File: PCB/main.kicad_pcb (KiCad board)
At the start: 2 copper layers, 51 parts, among them J1 S20B-PADSS-1, J2 S20B-PADSS-1, J3 SWD, SW1 SPST, U1 LM2596-5.0, U2 XC6206P33, U3 MCP2558FD, U4 MCP2558FD, U5 STM32G0B1, Y1 40M

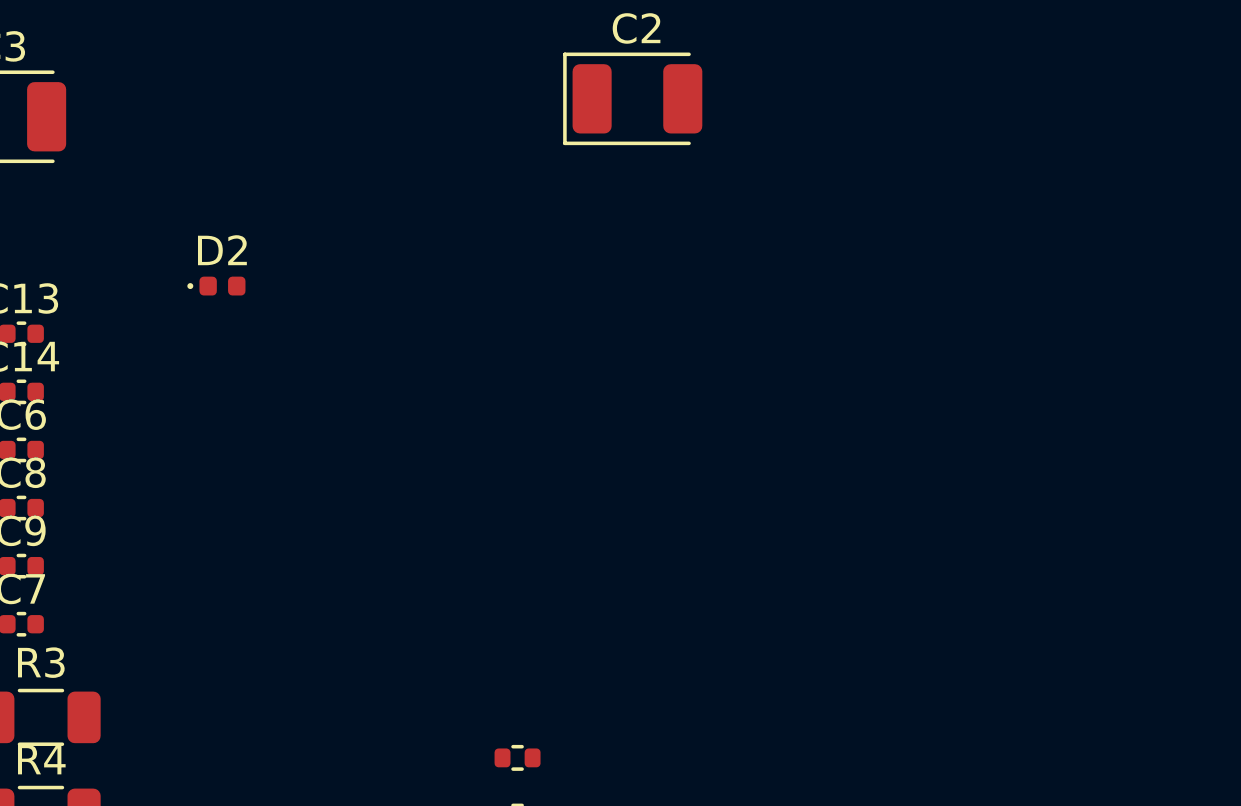
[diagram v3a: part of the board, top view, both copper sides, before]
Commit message: Add fuse holder
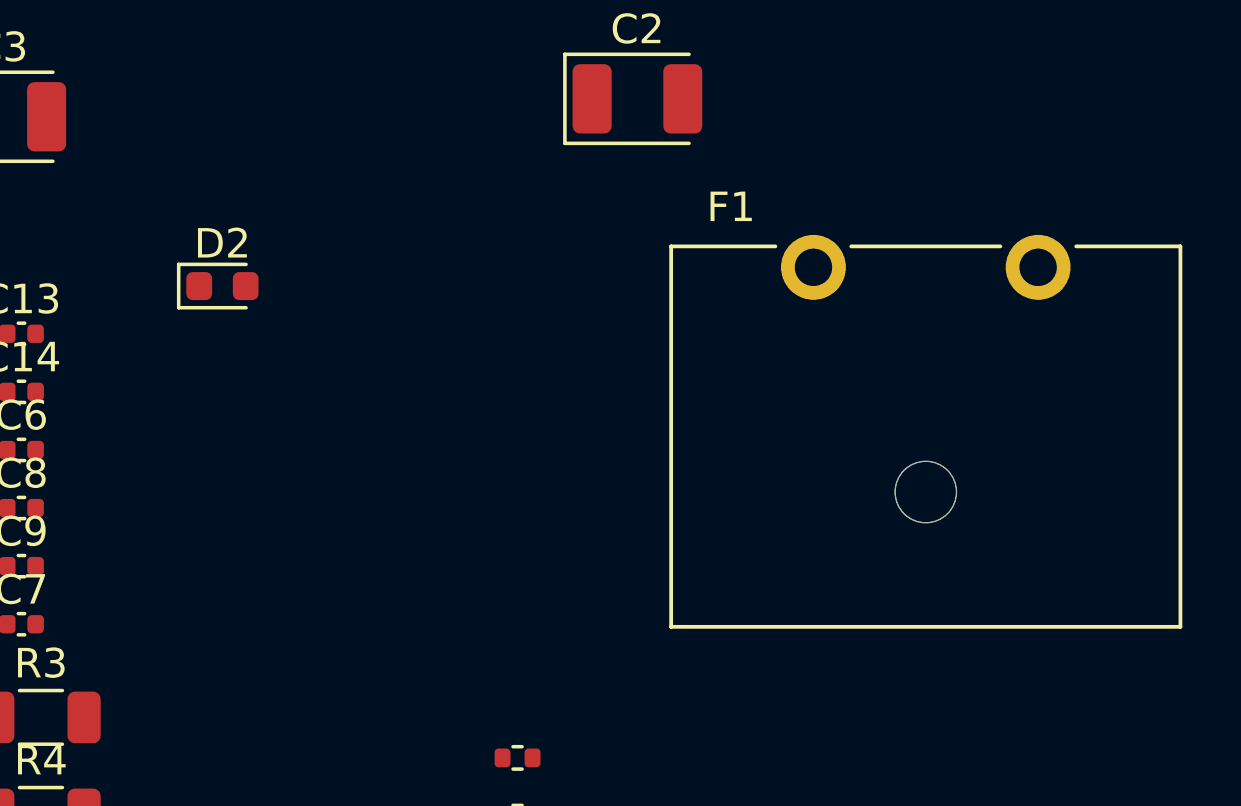
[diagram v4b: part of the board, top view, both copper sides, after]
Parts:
- added F1: Fuse, libdb:CMP-0026, F.Cu at (91.4, 35.6)
- D2: footprint LED_SMD:LED_0402_1005Metric -> LED_SMD:LED_0603_1608Metric
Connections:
- J1 pad 10: +BATT -> /JST_10_BAT+
- J2 pad 1: +BATT -> /JST_10_BAT+
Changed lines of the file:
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@@
   (net 82 "unconnected-(U5-PB8-Pad47)")
   (net 83 "unconnected-(U5-PB9-Pad48)")
+  (net 84 "/JST_10_BAT+")
   (footprint "Package_TO_SOT_SMD:TO-263-5_TabPin3" (layer "F.Cu")
     (at 28.841 47.733)
@@
     )
   )
-  (footprint "LED_SMD:LED_0402_1005Metric" (layer "F.Cu")
+  (footprint "LED_SMD:LED_0603_1608Metric" (layer "F.Cu")
     (at 67.587 28.575)
-    (descr "LED SMD 0402 (1005 Metric), square (rectangular) end terminal, IPC_7351 nominal, (Body size source: http://www.tortai-tech.com/upload/download/2011102023233369053.pdf), generated with kicad-footprint-generator")
+    (descr "LED SMD 0603 (1608 Metric), square (rectangular) end terminal, IPC_7351 nominal, (Body size source: http://www.tortai-tech.com/upload/download/2011102023233369053.pdf), generated with kicad-footprint-generator")
     (tags "LED")
     (property "Case/Package Size" "0603")
@@
     (property "ki_keywords" "LED diode light-emitting-diode")
     (attr smd)
-    (fp_text reference "D2" (at 0 -1.17) (layer "F.SilkS")
+    (fp_text reference "D2" (at 0 -1.43) (layer "F.SilkS")
         (effects (font (size 1 1) (thickness 0.15)))
     )
-    (fp_text value "LED_B" (at 0 1.17) (layer "F.Fab")
+    (fp_text value "LED_B" (at 0 1.43) (layer "F.Fab")
         (effects (font (size 1 1) (thickness 0.15)))
     )
     (fp_text user "${REFERENCE}" (at 0 0) (layer "F.Fab")
-        (effects (font (size 0.25 0.25) (thickness 0.04)))
+        (effects (font (size 0.4 0.4) (thickness 0.06)))
     )
-    (fp_circle (center -1.09 0) (end -1.04 0)
-      (stroke (width 0.1) (type solid)) (fill none) (layer "F.SilkS"))
-    (fp_line (start -0.93 -0.47) (end 0.93 -0.47)
+    (fp_line (start -1.485 -0.735) (end -1.485 0.735)
+      (stroke (width 0.12) (type solid)) (layer "F.SilkS"))
+    (fp_line (start -1.485 0.735) (end 0.8 0.735)
+      (stroke (width 0.12) (type solid)) (layer "F.SilkS"))
+    (fp_line (start 0.8 -0.735) (end -1.485 -0.735)
+      (stroke (width 0.12) (type solid)) (layer "F.SilkS"))
+    (fp_line (start -1.48 -0.73) (end 1.48 -0.73)
       (stroke (width 0.05) (type solid)) (layer "F.CrtYd"))
-    (fp_line (start -0.93 0.47) (end -0.93 -0.47)
+    (fp_line (start -1.48 0.73) (end -1.48 -0.73)
       (stroke (width 0.05) (type solid)) (layer "F.CrtYd"))
-    (fp_line (start 0.93 -0.47) (end 0.93 0.47)
+    (fp_line (start 1.48 -0.73) (end 1.48 0.73)
       (stroke (width 0.05) (type solid)) (layer "F.CrtYd"))
-    (fp_line (start 0.93 0.47) (end -0.93 0.47)
+    (fp_line (start 1.48 0.73) (end -1.48 0.73)
       (stroke (width 0.05) (type solid)) (layer "F.CrtYd"))
-    (fp_line (start -0.5 -0.25) (end 0.5 -0.25)
+    (fp_line (start -0.8 -0.1) (end -0.8 0.4)
       (stroke (width 0.1) (type solid)) (layer "F.Fab"))
-    (fp_line (start -0.5 0.25) (end -0.5 -0.25)
+    (fp_line (start -0.8 0.4) (end 0.8 0.4)
       (stroke (width 0.1) (type solid)) (layer "F.Fab"))
-    (fp_line (start -0.4 0.25) (end -0.4 -0.25)
+    (fp_line (start -0.5 -0.4) (end -0.8 -0.1)
       (stroke (width 0.1) (type solid)) (layer "F.Fab"))
-    (fp_line (start -0.3 0.25) (end -0.3 -0.25)
+    (fp_line (start 0.8 -0.4) (end -0.5 -0.4)
       (stroke (width 0.1) (type solid)) (layer "F.Fab"))
-    (fp_line (start 0.5 -0.25) (end 0.5 0.25)
+    (fp_line (start 0.8 0.4) (end 0.8 -0.4)
       (stroke (width 0.1) (type solid)) (layer "F.Fab"))
-    (fp_line (start 0.5 0.25) (end -0.5 0.25)
-      (stroke (width 0.1) (type solid)) (layer "F.Fab"))
-    (pad "1" smd roundrect (at -0.485 0) (size 0.59 0.64) (layers "F.Cu" "F.Paste" "F.Mask") (roundrect_rratio 0.25)
+    (pad "1" smd roundrect (at -0.7875 0) (size 0.875 0.95) (layers "F.Cu" "F.Paste" "F.Mask") (roundrect_rratio 0.25)
       (net 1 "Earth") (pinfunction "K") (pintype "passive"))
-    (pad "2" smd roundrect (at 0.485 0) (size 0.59 0.64) (layers "F.Cu" "F.Paste" "F.Mask") (roundrect_rratio 0.25)
+    (pad "2" smd roundrect (at 0.7875 0) (size 0.875 0.95) (layers "F.Cu" "F.Paste" "F.Mask") (roundrect_rratio 0.25)
       (net 51 "Net-(D2-A)") (pinfunction "A") (pintype "passive"))
-    (model "${KICAD6_3DMODEL_DIR}/LED_SMD.3dshapes/LED_0402_1005Metric.wrl"
+    (model "${KICAD6_3DMODEL_DIR}/LED_SMD.3dshapes/LED_0603_1608Metric.wrl"
       (offset (xyz 0 0 0))
       (scale (xyz 1 1 1))
@@
     (pad "" np_thru_hole circle (at -3.4 19.6) (size 1.1 1.1) (drill 1.1) (layers "F&B.Cu" "*.Mask"))
     (pad "1" thru_hole rect (at 0 0) (size 1.35 1.35) (drill 0.8) (layers "*.Cu" "*.Mask")
-      (net 37 "+BATT") (pinfunction "Pin_1") (pintype "passive"))
+      (net 84 "/JST_10_BAT+") (pinfunction "Pin_1") (pintype "passive"))
     (pad "2" thru_hole oval (at 0 2) (size 1.35 1.35) (drill 0.8) (layers "*.Cu" "*.Mask")
       (net 1 "Earth") (pinfunction "Pin_2") (pintype "passive"))
@@
     )
   )
+  (footprint "libdb:CMP-0026" (layer "F.Cu")
+    (at 91.44 35.56)
+    (property "LCSC" "LCSC: C206906")
+    (property "MPN" "01530007Z")
+    (property "Manufacturer" "Littelfuse")
+    (property "Rating" "")
+    (property "Sheetfile" "main.kicad_sch")
+    (property "Sheetname" "")
+    (property "ki_description" "Fuse Holder Inline Horizontal Mount")
+    (property "ki_keywords" "fuse")
+    (attr through_hole)
+    (fp_text reference "F1" (at -6.604 -9.652) (layer "F.SilkS")
+        (effects (font (size 1 1) (thickness 0.15)))
+    )
+    (fp_text value "Fuse" (at -4.064 3.556) (layer "F.Fab")
+        (effects (font (size 1 1) (thickness 0.15)))
+    )
+    (fp_line (start -8.636 -8.3312) (end -8.636 4.572)
+      (stroke (width 0.127) (type solid)) (layer "F.SilkS"))
+    (fp_line (start -8.636 4.572) (end 8.636 4.572)
+      (stroke (width 0.127) (type solid)) (layer "F.SilkS"))
+    (fp_line (start -5.1 -8.3312) (end -8.636 -8.3312)
+      (stroke (width 0.127) (type solid)) (layer "F.SilkS"))
+    (fp_line (start 2.53 -8.3312) (end -2.53 -8.3312)
+      (stroke (width 0.127) (type solid)) (layer "F.SilkS"))
+    (fp_line (start 8.636 -8.3312) (end 5.1 -8.3312)
+      (stroke (width 0.127) (type solid)) (layer "F.SilkS"))
+    (fp_line (start 8.636 4.572) (end 8.636 -8.3312)
+      (stroke (width 0.127) (type solid)) (layer "F.SilkS"))
+    (fp_line (start -8.886 -8.8312) (end 8.886 -8.8312)
+      (stroke (width 0.05) (type solid)) (layer "F.CrtYd"))
+    (fp_line (start -8.886 10.541) (end -8.886 -8.8312)
+      (stroke (width 0.05) (type solid)) (layer "F.CrtYd"))
+    (fp_line (start 8.886 -8.8312) (end 8.886 10.541)
+      (stroke (width 0.05) (type solid)) (layer "F.CrtYd"))
+    (fp_line (start 8.886 10.541) (end -8.886 10.541)
+      (stroke (width 0.05) (type solid)) (layer "F.CrtYd"))
+    (fp_line (start -8.636 -8.3312) (end 8.636 -8.3312)
+      (stroke (width 0.127) (type solid)) (layer "F.Fab"))
+    (fp_line (start -8.636 4.572) (end -8.636 -8.3312)
+      (stroke (width 0.127) (type solid)) (layer "F.Fab"))
+    (fp_line (start 8.636 -8.3312) (end 8.636 4.572)
+      (stroke (width 0.127) (type solid)) (layer "F.Fab"))
+    (fp_line (start 8.636 4.572) (end -8.636 4.572)
+      (stroke (width 0.127) (type solid)) (layer "F.Fab"))
+    (pad "" np_thru_hole circle (at 0 0) (size 2.0828 2.0828) (drill 2.0828) (layers "*.Cu" "*.Mask"))
+    (pad "1" thru_hole circle (at -3.81 -7.62) (size 2.2 2.2) (drill 1.27) (layers "*.Cu" "*.Mask")
+      (net 37 "+BATT") (pintype "passive"))
+    (pad "2" thru_hole circle (at 3.81 -7.62) (size 2.2 2.2) (drill 1.27) (layers "*.Cu" "*.Mask")
+      (net 84 "/JST_10_BAT+") (pintype "passive"))
+    (model "../libdb.3dshapes/CMP-0026.step"
+      (offset (xyz 0 2.1 0))
+      (scale (xyz 1 1 1))
+      (rotate (xyz -90 0 90))
+    )
+  )
   (footprint "Capacitor_SMD:C_0402_1005Metric" (layer "F.Cu")
     (at 60.771 38.073)
@@
       (net 1 "Earth") (pinfunction "Pin_9") (pintype "passive"))
     (pad "10" thru_hole oval (at 0 18) (size 1.35 1.35) (drill 0.8) (layers "*.Cu" "*.Mask")
-      (net 37 "+BATT") (pinfunction "Pin_10") (pintype "passive"))
+      (net 84 "/JST_10_BAT+") (pinfunction "Pin_10") (pintype "passive"))
     (pad "11" thru_hole oval (at -2 0) (size 1.35 1.35) (drill 0.8) (layers "*.Cu" "*.Mask")
       (net 23 "/JST_11_AUDIO_FL") (pinfunction "Pin_11") (pintype "passive"))

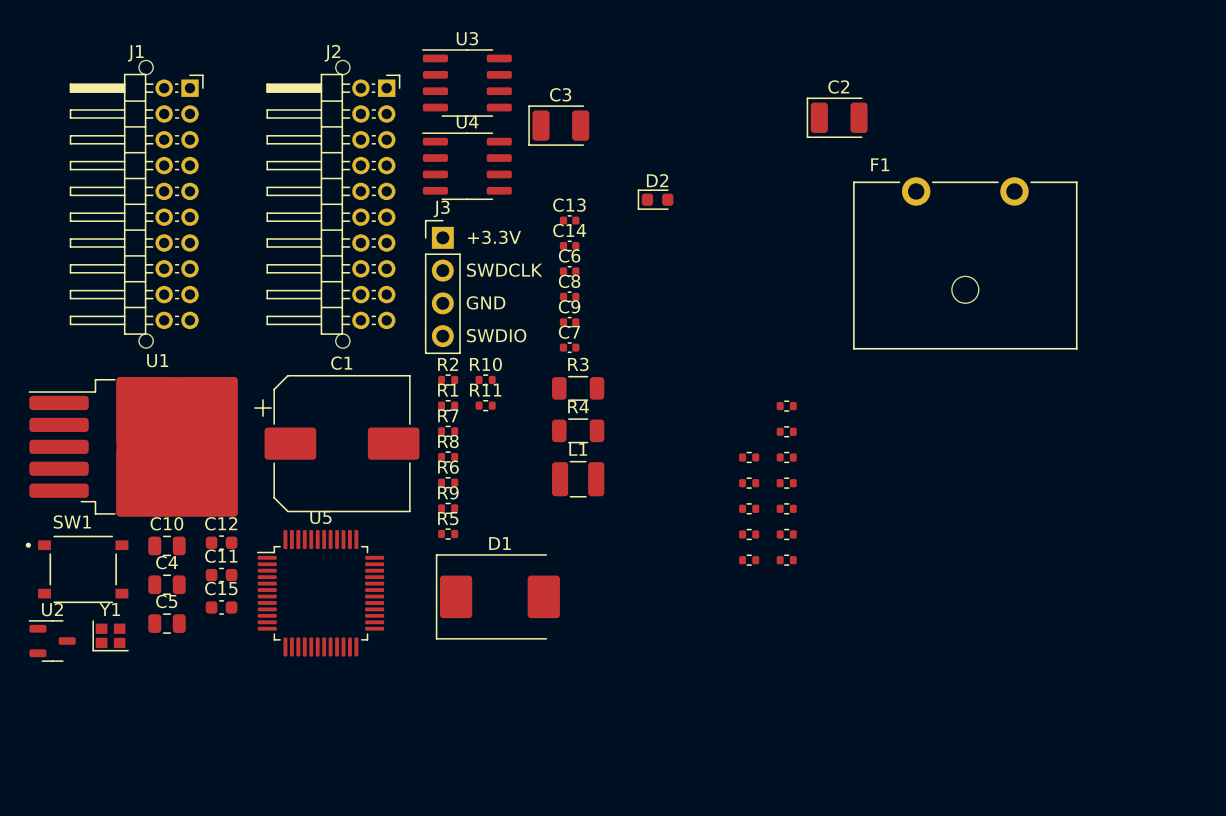
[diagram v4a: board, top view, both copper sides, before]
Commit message: Change buck converter
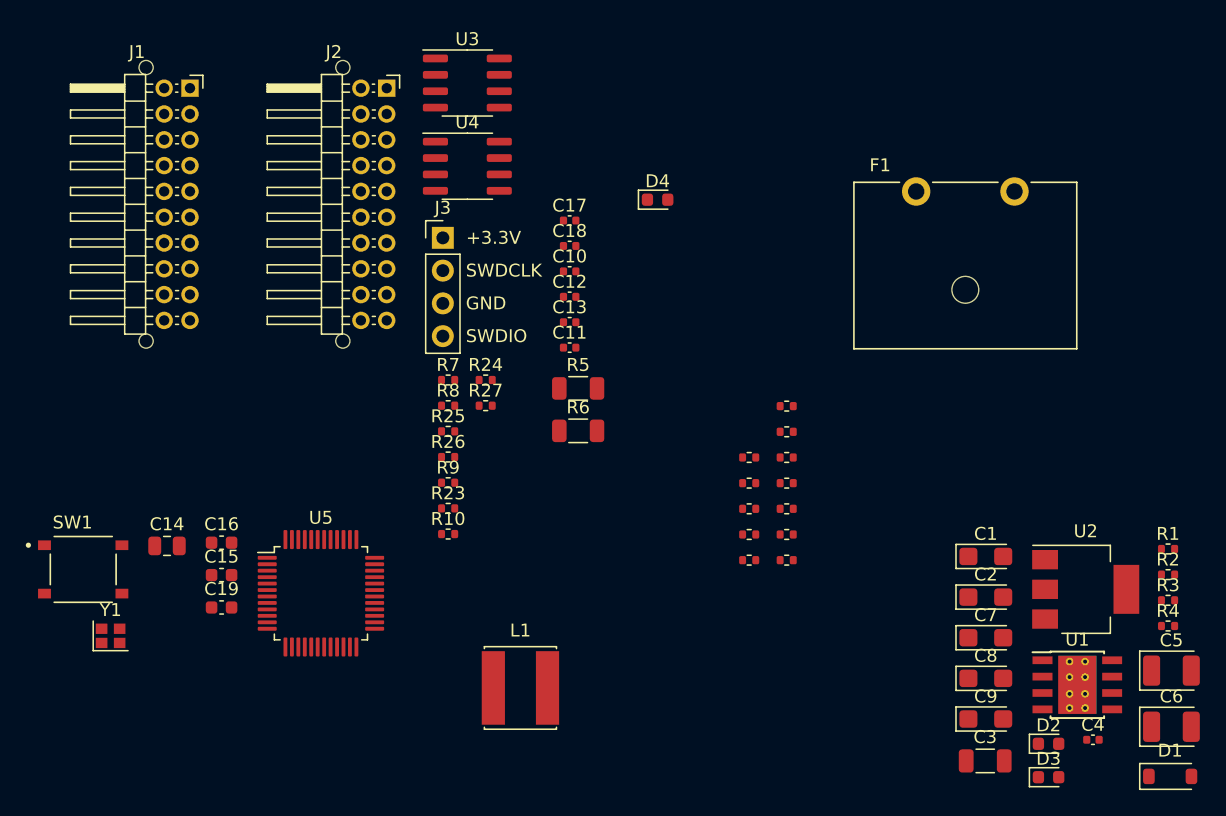
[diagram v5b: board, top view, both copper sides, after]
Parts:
- added C6: 100u, Capacitor_Tantalum_SMD:CP_EIA-3528-15_AVX-H, F.Cu at (107.4, 69.4)
- added C7: 10u, Capacitor_Tantalum_SMD:CP_EIA-3216-18_Kemet-A, F.Cu at (93.0, 62.5)
- added C8: 10u, Capacitor_Tantalum_SMD:CP_EIA-3216-18_Kemet-A, F.Cu at (93.0, 65.7)
- added C9: 10u, Capacitor_Tantalum_SMD:CP_EIA-3216-18_Kemet-A, F.Cu at (93.0, 68.8)
- added D2: LED_B, LED_SMD:LED_0603_1608Metric, F.Cu at (97.9, 70.7)
- added D3: LED_B, LED_SMD:LED_0603_1608Metric, F.Cu at (97.9, 73.3)
- added R1: 6.8k, Resistor_SMD:R_0402_1005Metric, F.Cu at (107.2, 55.6)
- added R2: 2.2k, Resistor_SMD:R_0402_1005Metric, F.Cu at (107.2, 57.6)
- added R3: 470, Resistor_SMD:R_0402_1005Metric, F.Cu at (107.2, 59.6)
- added R4: 100, Resistor_SMD:R_0402_1005Metric, F.Cu at (107.2, 61.6)
- C1: value 330u -> 10u; footprint Capacitor_SMD:CP_Elec_10x10 -> Capacitor_Tantalum_SMD:CP_EIA-3216-18_Kemet-A
- C2: value 100u -> 10u; footprint Capacitor_Tantalum_SMD:CP_EIA-3528-15_AVX-H -> Capacitor_Tantalum_SMD:CP_EIA-3216-18_Kemet-A
- C3: value 100u -> 22u; footprint Capacitor_Tantalum_SMD:CP_EIA-3528-15_AVX-H -> Capacitor_SMD:C_1206_3216Metric
- C4: value 1u -> 10n; footprint Capacitor_SMD:C_0805_2012Metric -> Capacitor_SMD:C_0402_1005Metric
- C5: value 1u -> 100u; footprint Capacitor_SMD:C_0805_2012Metric -> Capacitor_Tantalum_SMD:CP_EIA-3528-15_AVX-H
- D1: value SS36 -> B5819W; footprint Diode_SMD:D_SMC -> Diode_SMD:D_SOD-123
- L1: footprint Inductor_SMD:L_1210_3225Metric -> libdb:CMP-0036
- U1: value LM2596-5.0 -> TPS5430; footprint Package_TO_SOT_SMD:TO-263-5_TabPin3 -> Package_SO:TI_SO-PowerPAD-8_ThermalVias
- U2: value XC6206P33 -> AMS1117-3.3; footprint libdb:CMP-0019 -> Package_TO_SOT_SMD:SOT-223-3_TabPin2
- moved U2 80.2 mm to (100.8, 58.8)
- moved C5 77.9 mm to (107.4, 65.1)
- moved U1 73.6 mm to (100.1, 66.2)
- moved C4 72.8 mm to (101.3, 70.4)
- moved C3 59.2 mm to (93.0, 72.1)
- moved D1 53.8 mm to (107.3, 73.3)
- moved C1 50.7 mm to (93.0, 56.2)
- moved C2 38.9 mm to (93.0, 59.4)
- moved L1 16.8 mm to (57.0, 66.4)
- renumbered C6 to C10, C7 to C11, C8 to C12, C9 to C13, C10 to C14, C11 to C15, C12 to C16, C13 to C17, C14 to C18, C15 to C19, D2 to D4, R5 to R10, R12 to R11, R13 to R12, R14 to R13, R15 to R14, R16 to R15, R17 to R16, R18 to R17, R19 to R18, R20 to R19, R21 to R20, R22 to R21, R23 to R22, R9 to R23, R10 to R24, R7 to R25, R8 to R26, R11 to R27, R3 to R5, R4 to R6, R2 to R7, R1 to R8, R6 to R9
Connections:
- C17 pad 1: Earth -> /XTAL2
- C17 pad 2: Net-(U5-PF0) -> Earth
- C18 pad 1: Earth -> /XTAL1
- C18 pad 2: Net-(U5-PF1) -> Earth
- C2 pad 1: +5V -> +BATT
- C3 pad 1: +5V -> +BATT
- C4 pad 1: +5V -> Net-(U1-BOOT)
- C4 pad 2: Earth -> Net-(D1-K)
- C5 pad 1: +3.3V -> +5V
- U1 pad 1: +BATT -> Net-(U1-BOOT)
- U1 pad 2: Net-(D1-K) -> unconnected-(U1-NC-Pad2)
- U1 pad 3: Earth -> unconnected-(U1-NC-Pad3)
- U1 pad 4: +5V -> Net-(U1-VSENSE)
- U1 pad 5: Earth -> unconnected-(U1-EN-Pad5)
- U5 pad 8: Net-(U5-PF0) -> /XTAL1
- U5 pad 9: Net-(U5-PF1) -> /XTAL2
- Y1 pad 1: Net-(U5-PF0) -> /XTAL1
- Y1 pad 3: Net-(U5-PF1) -> /XTAL2

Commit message: Continue development
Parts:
- added ART1: Cat (small, mirrored), libdb:CMP-0044, F.Cu at (72.1, 72.6)
- added ART2: Dog (small), libdb:CMP-0045, F.Cu at (78.7, 71.1)
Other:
- board text added: "1A Mini-Blade"
